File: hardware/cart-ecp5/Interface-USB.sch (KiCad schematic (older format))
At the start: 40 parts, among them U3 USBLC6-2SC6

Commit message: Replace FT2232HL with FT2232HQ for QFN-64 package
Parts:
- removed U?: FT2232HL, Package_QFP:LQFP-64_10x10mm_P0.5mm, symbol ng_ftdi:FT2232H
- added U?: FT2232HQ, Package_DFN_QFN:QFN-64-1EP_9x9mm_P0.5mm_EP4.35x4.35mm, symbol ng_ftdi:FT2232HQ
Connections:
- wire segments 191 -> 193
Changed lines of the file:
@@
 Connection ~ 9150 1350
 Wire Wire Line
-	9200 5850 9200 5950
-Wire Wire Line
-	9200 5950 9100 5950
+	9150 5850 9150 5950
+Wire Wire Line
+	9150 5950 9050 5950
 Wire Wire Line
 	7450 5550 7550 5550
 Wire Wire Line
-	8300 5850 8300 5950
-Connection ~ 8300 5950
-Wire Wire Line
-	8500 5850 8500 5950
-Connection ~ 8500 5950
-Wire Wire Line
-	8600 5850 8600 5950
-Connection ~ 8600 5950
-Wire Wire Line
-	8600 5950 8500 5950
-Wire Wire Line
-	8700 5850 8700 5950
-Connection ~ 8700 5950
-Wire Wire Line
-	8700 5950 8600 5950
-Wire Wire Line
-	8800 5850 8800 5950
-Connection ~ 8800 5950
-Wire Wire Line
-	8800 5950 8700 5950
-Wire Wire Line
-	8900 5850 8900 5950
-Connection ~ 8900 5950
-Wire Wire Line
-	8900 5950 8800 5950
-Wire Wire Line
-	9000 5850 9000 5950
-Connection ~ 9000 5950
-Wire Wire Line
-	9000 5950 8900 5950
-Wire Wire Line
-	9100 5850 9100 5950
-Connection ~ 9100 5950
-Wire Wire Line
-	9100 5950 9000 5950
+	8250 5850 8250 5950
+Connection ~ 8250 5950
+Wire Wire Line
+	8450 5850 8450 5950
+Connection ~ 8450 5950
+Wire Wire Line
+	8550 5850 8550 5950
+Connection ~ 8550 5950
+Wire Wire Line
+	8550 5950 8450 5950
+Wire Wire Line
+	8650 5850 8650 5950
+Connection ~ 8650 5950
+Wire Wire Line
+	8650 5950 8550 5950
+Wire Wire Line
+	8750 5850 8750 5950
+Connection ~ 8750 5950
+Wire Wire Line
+	8750 5950 8650 5950
+Wire Wire Line
+	8850 5850 8850 5950
+Connection ~ 8850 5950
+Wire Wire Line
+	8850 5950 8750 5950
+Wire Wire Line
+	8950 5850 8950 5950
+Connection ~ 8950 5950
+Wire Wire Line
+	8950 5950 8850 5950
+Wire Wire Line
+	9050 5850 9050 5950
+Connection ~ 9050 5950
+Wire Wire Line
+	9050 5950 8950 5950
 NoConn ~ 7550 5050
 NoConn ~ 9950 5350
@@
 Connection ~ 8950 1350
 Wire Wire Line
-	8500 5950 8300 5950
-Wire Wire Line
-	8300 5950 8300 6050
+	8450 5950 8250 5950
+Wire Wire Line
+	8250 5950 8250 6050
 Wire Wire Line
 	7450 5550 7450 5650
@@
 Wire Wire Line
 	4300 6400 4300 6500
-$Comp
-L ng_ftdi:FT2232H U?
-U 1 1 5F212584
-P 8750 3650
-F 0 "U?" H 7700 5850 50  0000 L CNN
-F 1 "FT2232HL" H 7700 5750 50  0000 L CNN
-F 2 "Package_QFP:LQFP-64_10x10mm_P0.5mm" H 8750 3650 50  0001 C CNN
-F 3 "https://www.ftdichip.com/Support/Documents/DataSheets/ICs/DS_FT2232H.pdf" H 8750 3650 50  0001 C CNN
-	1    8750 3650
-	1    0    0    -1
-$EndComp
 Wire Wire Line
 	7450 2950 7550 2950
@@
 L ng_power:GND #PWR0113
 U 1 1 5F44E9B1
-P 8300 6050
+P 8250 6050
 AR Path="/5F44E9B1" Ref="#PWR0113"  Part="1"
 AR Path="/5F302051/5F44E9B1" Ref="#PWR?"  Part="1"
 AR Path="/5F4552C5/5F44E9B1" Ref="#PWR?"  Part="1"
-F 0 "#PWR?" H 8300 5800 50  0001 C CNN
-F 1 "GND" H 8303 5924 50  0000 C CNN
-F 2 "" H 8200 5700 50  0001 C CNN
-F 3 "" H 8300 6050 50  0001 C CNN
-	1    8300 6050
+F 0 "#PWR?" H 8250 5800 50  0001 C CNN
+F 1 "GND" H 8253 5924 50  0000 C CNN
+F 2 "" H 8150 5700 50  0001 C CNN
+F 3 "" H 8250 6050 50  0001 C CNN
+	1    8250 6050
 	1    0    0    -1
 $EndComp
@@
 	1    0    0    -1
 $EndComp
+$Comp
+L ng_ftdi:FT2232HQ U?
+U 1 1 5F48BD9E
+P 8750 3650
+F 0 "U?" H 7700 5850 50  0000 L CNN
+F 1 "FT2232HQ" H 7700 5750 50  0000 L CNN
+F 2 "Package_DFN_QFN:QFN-64-1EP_9x9mm_P0.5mm_EP4.35x4.35mm" H 8750 3650 50  0001 C CNN
+F 3 "https://www.ftdichip.com/Support/Documents/DataSheets/ICs/DS_FT2232H.pdf" H 8750 3650 50  0001 C CNN
+	1    8750 3650
+	1    0    0    -1
+$EndComp
+Wire Wire Line
+	9150 5950 9250 5950
+Wire Wire Line
+	9250 5950 9250 5850
+Connection ~ 9150 5950
 $EndSCHEMATC

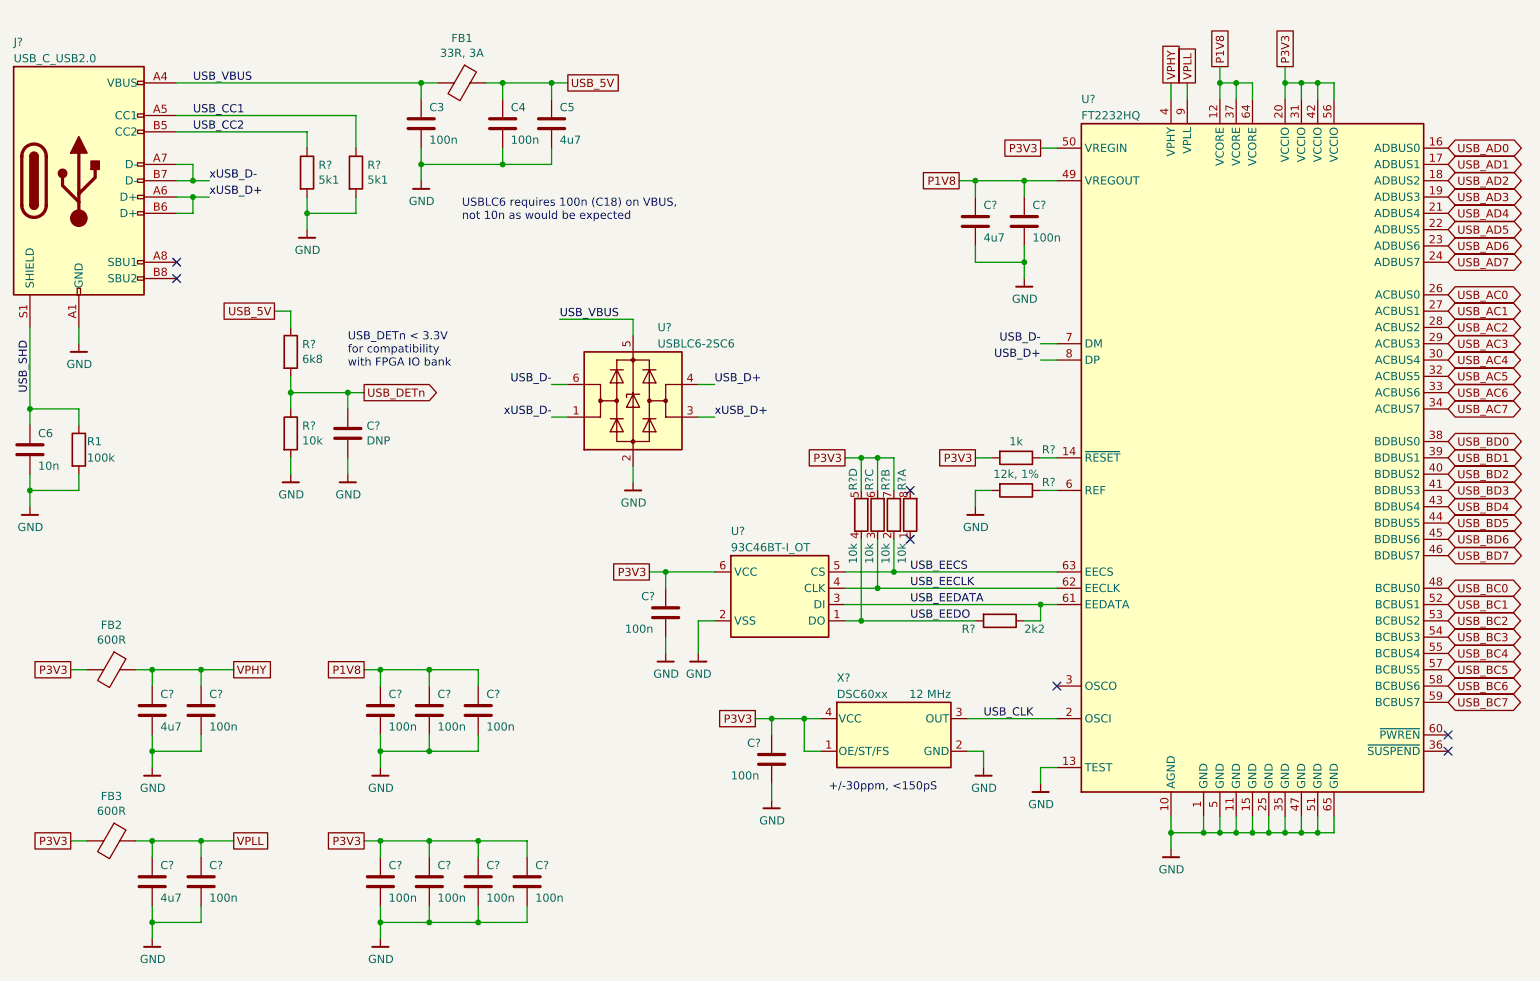
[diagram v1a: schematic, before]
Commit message: First pass annotation and footprint assignment complete
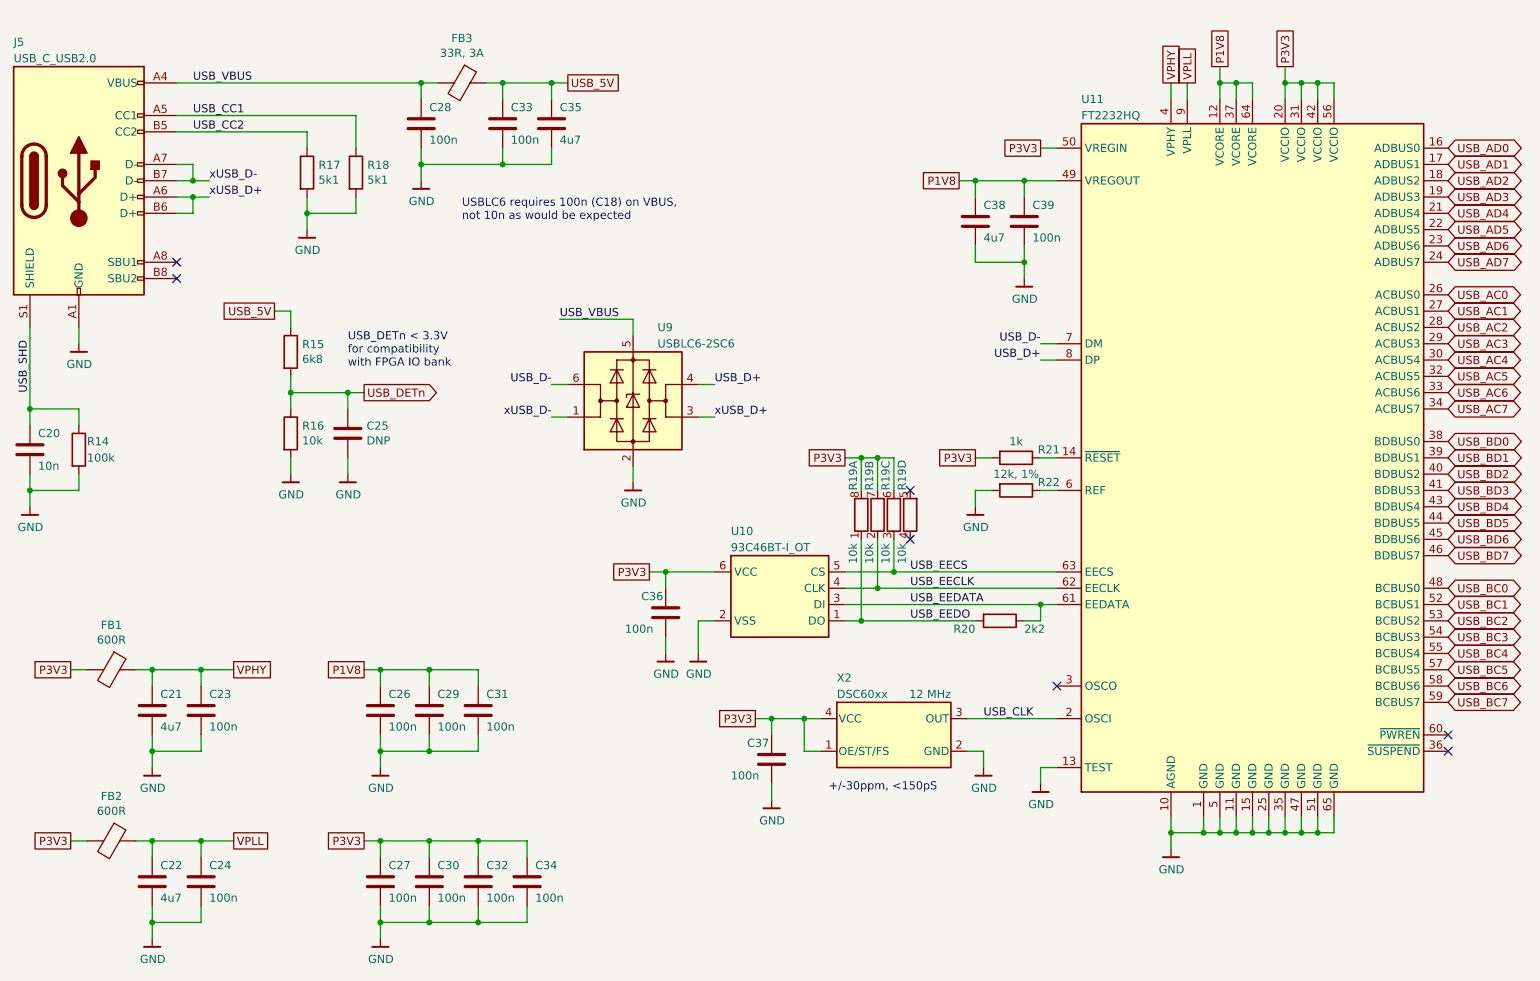
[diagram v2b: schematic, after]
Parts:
- gave numbers to parts that had none: 26
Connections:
- net P3V3: now also R19.6 (R3.2), R19.7 (R2.2), R19.8 (R1.2); no longer R19.5 (R4.2), R19.6 (R3.2), R19.7 (R2.2)
- net USB_EECLK: now also R19.2 (R2.1); no longer R19.3 (R3.1)
- net USB_EECS: now also R19.3 (R3.1); no longer R19.2 (R2.1)
- net USB_EEDO: now also R19.1 (R1.1); no longer R19.4 (R4.1)

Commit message: Initial placement pass
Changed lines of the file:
@@
 	5350 4650 5350 4850
 Wire Wire Line
-	6350 3650 6250 3650
-Connection ~ 6450 3650
-Wire Wire Line
-	6350 3650 6350 3850
-Wire Wire Line
-	6450 3650 6550 3650
-Wire Wire Line
-	6450 3650 6450 3850
-Wire Wire Line
-	6350 3650 6450 3650
-Wire Wire Line
-	6550 3850 6550 3650
+	6350 3550 6250 3550
+Connection ~ 6450 3550
+Wire Wire Line
+	6350 3550 6350 3850
+Wire Wire Line
+	6450 3550 6550 3550
+Wire Wire Line
+	6450 3550 6450 3850
+Wire Wire Line
+	6350 3550 6450 3550
+Wire Wire Line
+	6550 3850 6550 3550
 Wire Wire Line
 	6450 4450 6450 4150
@@
 Wire Wire Line
 	6250 4350 6550 4350
-Connection ~ 6350 3650
+Connection ~ 6350 3550
 Wire Wire Line
 	7550 4550 7450 4550
@@
 Text GLabel 3300 6000 0    50   UnSpc ~ 0
 P3V3
-Text GLabel 6250 3650 0    50   UnSpc ~ 0
+Text GLabel 6250 3550 0    50   UnSpc ~ 0
 P3V3
 $Comp

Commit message: Shrink smallest passive to 0402
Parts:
- C23, C24, C25, C26, C27, C29, C3, C30, C31, C32, C34, C36, C37, C39, C4, C6: footprint Capacitor_SMD:C_0603_1608Metric -> Capacitor_SMD:C_0402_1005Metric
- FB1: value 33R, 3A -> 33R; footprint Inductor_SMD:L_0603_1608Metric -> Inductor_SMD:L_0402_1005Metric; MPN BLM18PG330SN1D -> (none)
- FB2, FB3: footprint Inductor_SMD:L_0603_1608Metric -> Inductor_SMD:L_0402_1005Metric
- R1: footprint Resistor_SMD:R_0603_1608Metric -> Resistor_SMD:R_0402_1005Metric; MPN RC0603JR-07100KL -> (none)
- R17, R18, R20, R21, R22: footprint Resistor_SMD:R_0603_1608Metric -> Resistor_SMD:R_0402_1005Metric
- R19: footprint Resistor_SMD:R_Array_Convex_4x0603 -> Resistor_SMD:R_0402_1005Metric; symbol Device:R_Pack04_Split -> Device:R; MPN YC164-JR-0710KL -> (none)
- R23, R24: renamed from R19; footprint Resistor_SMD:R_Array_Convex_4x0603 -> Resistor_SMD:R_0402_1005Metric; symbol Device:R_Pack04_Split -> Device:R
- R25: renamed from R19; footprint Resistor_SMD:R_Array_Convex_4x0603 -> Resistor_SMD:R_0402_1005Metric; symbol Device:R_Pack04_Split -> Device:R; MPN YC164-JR-0710KL -> (none)
- R3: footprint Resistor_SMD:R_0603_1608Metric -> Resistor_SMD:R_0402_1005Metric; MPN RC0603FR-076K8L -> (none)
- R5: footprint Resistor_SMD:R_0603_1608Metric -> Resistor_SMD:R_0402_1005Metric; MPN RC0603FR-0710KL -> (none)
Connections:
- net P3V3: now also R19.1, R23.1, R24.1; no longer R19.8 (R1.2), R23.7 (R2.2), R24.6 (R3.2)
- net USB_EECS: now also R24.2; no longer R24.3 (R3.1)
- net USB_EEDO: now also R19.2; no longer R19.1 (R1.1)
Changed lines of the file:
@@
 U 1 1 5F1F46DB
 P 5150 4600
-F 0 "C36" H 5000 4700 50  0000 L CNN
+F 0 "C36" H 4950 4700 50  0000 L CNN
 F 1 "100n" H 4900 4500 50  0000 L CNN
-F 2 "Capacitor_SMD:C_0603_1608Metric" H 5188 4450 50  0001 C CNN
+F 2 "Capacitor_SMD:C_0402_1005Metric" H 5188 4450 50  0001 C CNN
 F 3 "~" H 5150 4600 50  0001 C CNN
 	1    5150 4600
@@
 	6550 4350 6550 4150
 $Comp
-L Device:R_Pack04_Split R19
-U 4 1 5F1F46F9
+L Device:R R25
+U 1 1 5F1F46F9
 P 6650 4000
-F 0 "R19" V 6600 4150 50  0000 L CNN
+F 0 "R25" V 6600 4150 50  0000 L CNN
 F 1 "10k" V 6600 3700 50  0000 L CNN
-F 2 "Resistor_SMD:R_Array_Convex_4x0603" V 6580 4000 50  0001 C CNN
+F 2 "Resistor_SMD:R_0402_1005Metric" V 6580 4000 50  0001 C CNN
 F 3 "~" H 6650 4000 50  0001 C CNN
-F 4 "YC164-JR-0710KL" V 6650 4000 50  0001 C CNN "MPN"
-	4    6650 4000
-	1    0    0    -1
-$EndComp
-$Comp
-L Device:R_Pack04_Split R19
-U 2 1 5F1F46FF
+F 4 "" V 6650 4000 50  0001 C CNN "MPN"
+	1    6650 4000
+	1    0    0    -1
+$EndComp
+$Comp
+L Device:R R23
+U 1 1 5F1F46FF
 P 6450 4000
-F 0 "R19" V 6400 4150 50  0000 L CNN
+F 0 "R23" V 6400 4150 50  0000 L CNN
 F 1 "10k" V 6400 3700 50  0000 L CNN
-F 2 "Resistor_SMD:R_Array_Convex_4x0603" V 6380 4000 50  0001 C CNN
+F 2 "Resistor_SMD:R_0402_1005Metric" V 6380 4000 50  0001 C CNN
 F 3 "~" H 6450 4000 50  0001 C CNN
-	2    6450 4000
-	1    0    0    -1
-$EndComp
-$Comp
-L Device:R_Pack04_Split R19
-U 3 1 5F1F4705
+	1    6450 4000
+	1    0    0    -1
+$EndComp
+$Comp
+L Device:R R24
+U 1 1 5F1F4705
 P 6550 4000
-F 0 "R19" V 6500 4150 50  0000 L CNN
+F 0 "R24" V 6500 4150 50  0000 L CNN
 F 1 "10k" V 6500 3700 50  0000 L CNN
-F 2 "Resistor_SMD:R_Array_Convex_4x0603" V 6480 4000 50  0001 C CNN
+F 2 "Resistor_SMD:R_0402_1005Metric" V 6480 4000 50  0001 C CNN
 F 3 "~" H 6550 4000 50  0001 C CNN
-	3    6550 4000
+	1    6550 4000
 	1    0    0    -1
 $EndComp
@@
 U 1 1 5F1F476F
 P 5800 5500
-F 0 "C37" H 5650 5600 50  0000 L CNN
+F 0 "C37" H 5600 5600 50  0000 L CNN
 F 1 "100n" H 5550 5400 50  0000 L CNN
-F 2 "Capacitor_SMD:C_0603_1608Metric" H 5838 5350 50  0001 C CNN
+F 2 "Capacitor_SMD:C_0402_1005Metric" H 5838 5350 50  0001 C CNN
 F 3 "~" H 5800 5500 50  0001 C CNN
 	1    5800 5500
@@
 F 0 "C39" H 7300 2300 50  0000 R CNN
 F 1 "100n" H 7300 2100 50  0000 R CNN
-F 2 "Capacitor_SMD:C_0603_1608Metric" H 7388 2050 50  0001 C CNN
+F 2 "Capacitor_SMD:C_0402_1005Metric" H 7388 2050 50  0001 C CNN
 F 3 "~" H 7350 2200 50  0001 C CNN
 	1    7350 2200
@@
 F 0 "C23" H 2350 5300 50  0000 L CNN
 F 1 "100n" H 2350 5100 50  0000 L CNN
-F 2 "Capacitor_SMD:C_0603_1608Metric" H 2338 5050 50  0001 C CNN
+F 2 "Capacitor_SMD:C_0402_1005Metric" H 2338 5050 50  0001 C CNN
 F 3 "~" H 2300 5200 50  0001 C CNN
 	1    2300 5200
@@
 F 0 "R20" V 7250 4500 50  0000 R CNN
 F 1 "2k2" V 7250 4800 50  0000 L CNN
-F 2 "Resistor_SMD:R_0603_1608Metric" V 7130 4650 50  0001 C CNN
+F 2 "Resistor_SMD:R_0402_1005Metric" V 7130 4650 50  0001 C CNN
 F 3 "~" H 7200 4650 50  0001 C CNN
 	1    7200 4650
@@
 F 0 "C33" H 4200 1700 50  0000 L CNN
 F 1 "100n" H 4200 1500 50  0000 L CNN
-F 2 "Capacitor_SMD:C_0603_1608Metric" H 4188 1450 50  0001 C CNN
+F 2 "Capacitor_SMD:C_0402_1005Metric" H 4188 1450 50  0001 C CNN
 F 3 "~" H 4150 1600 50  0001 C CNN
 F 4 "" H 4150 1600 50  0001 C CNN "MPN"
@@
 F 0 "R14" H 1600 3650 50  0000 L CNN
 F 1 "100k" H 1600 3550 50  0000 L CNN
-F 2 "Resistor_SMD:R_0603_1608Metric" V 1480 3600 50  0001 C CNN
+F 2 "Resistor_SMD:R_0402_1005Metric" V 1480 3600 50  0001 C CNN
 F 3 "~" H 1550 3600 50  0001 C CNN
-F 4 "RC0603JR-07100KL" H 1550 3600 50  0001 C CNN "MPN"
+F 4 "" H 1550 3600 50  0001 C CNN "MPN"
 	1    1550 3600
 	1    0    0    -1
@@
 F 0 "C20" H 1300 3700 50  0000 L CNN
 F 1 "10n" H 1300 3500 50  0000 L CNN
-F 2 "Capacitor_SMD:C_0603_1608Metric" H 1288 3450 50  0001 C CNN
+F 2 "Capacitor_SMD:C_0402_1005Metric" H 1288 3450 50  0001 C CNN
 F 3 "~" H 1250 3600 50  0001 C CNN
 F 4 "" H 1250 3600 50  0001 C CNN "MPN"
@@
 AR Path="/5F4552C5/5F184C3D" Ref="FB3"  Part="1"
 F 0 "FB3" V 3626 1350 50  0000 C CNN
-F 1 "33R, 3A" V 3717 1350 50  0000 C CNN
-F 2 "Inductor_SMD:L_0603_1608Metric" V 3830 1350 50  0001 C CNN
+F 1 "33R" V 3717 1350 50  0000 C CNN
+F 2 "Inductor_SMD:L_0402_1005Metric" V 3830 1350 50  0001 C CNN
 F 3 "~" H 3900 1350 50  0001 C CNN
-F 4 "BLM18PG330SN1D" V 3900 1350 50  0001 C CNN "MPN"
 	1    3900 1350
 	0    1    1    0
@@
 F 0 "C28" H 3700 1700 50  0000 L CNN
 F 1 "100n" H 3700 1500 50  0000 L CNN
-F 2 "Capacitor_SMD:C_0603_1608Metric" H 3688 1450 50  0001 C CNN
+F 2 "Capacitor_SMD:C_0402_1005Metric" H 3688 1450 50  0001 C CNN
 F 3 "~" H 3650 1600 50  0001 C CNN
 F 4 "" H 3650 1600 50  0001 C CNN "MPN"
@@
 F 0 "C24" H 2350 6350 50  0000 L CNN
 F 1 "100n" H 2350 6150 50  0000 L CNN
-F 2 "Capacitor_SMD:C_0603_1608Metric" H 2338 6100 50  0001 C CNN
+F 2 "Capacitor_SMD:C_0402_1005Metric" H 2338 6100 50  0001 C CNN
 F 3 "~" H 2300 6250 50  0001 C CNN
 	1    2300 6250
@@
 F 0 "C26" H 3450 5300 50  0000 L CNN
 F 1 "100n" H 3450 5100 50  0000 L CNN
-F 2 "Capacitor_SMD:C_0603_1608Metric" H 3438 5050 50  0001 C CNN
+F 2 "Capacitor_SMD:C_0402_1005Metric" H 3438 5050 50  0001 C CNN
 F 3 "~" H 3400 5200 50  0001 C CNN
 	1    3400 5200
@@
 F 0 "C29" H 3750 5300 50  0000 L CNN
 F 1 "100n" H 3750 5100 50  0000 L CNN
-F 2 "Capacitor_SMD:C_0603_1608Metric" H 3738 5050 50  0001 C CNN
+F 2 "Capacitor_SMD:C_0402_1005Metric" H 3738 5050 50  0001 C CNN
 F 3 "~" H 3700 5200 50  0001 C CNN
 	1    3700 5200
@@
 F 0 "C31" H 4050 5300 50  0000 L CNN
 F 1 "100n" H 4050 5100 50  0000 L CNN
-F 2 "Capacitor_SMD:C_0603_1608Metric" H 4038 5050 50  0001 C CNN
+F 2 "Capacitor_SMD:C_0402_1005Metric" H 4038 5050 50  0001 C CNN
 F 3 "~" H 4000 5200 50  0001 C CNN
 	1    4000 5200
@@
 F 0 "C34" H 4350 6350 50  0000 L CNN
 F 1 "100n" H 4350 6150 50  0000 L CNN
-F 2 "Capacitor_SMD:C_0603_1608Metric" H 4338 6100 50  0001 C CNN
+F 2 "Capacitor_SMD:C_0402_1005Metric" H 4338 6100 50  0001 C CNN
 F 3 "~" H 4300 6250 50  0001 C CNN
 	1    4300 6250
@@
 F 0 "C32" H 4050 6350 50  0000 L CNN
 F 1 "100n" H 4050 6150 50  0000 L CNN
-F 2 "Capacitor_SMD:C_0603_1608Metric" H 4038 6100 50  0001 C CNN
+F 2 "Capacitor_SMD:C_0402_1005Metric" H 4038 6100 50  0001 C CNN
 F 3 "~" H 4000 6250 50  0001 C CNN
 	1    4000 6250
@@
 F 0 "C30" H 3750 6350 50  0000 L CNN
 F 1 "100n" H 3750 6150 50  0000 L CNN
-F 2 "Capacitor_SMD:C_0603_1608Metric" H 3738 6100 50  0001 C CNN
+F 2 "Capacitor_SMD:C_0402_1005Metric" H 3738 6100 50  0001 C CNN
 F 3 "~" H 3700 6250 50  0001 C CNN
 	1    3700 6250
@@
 F 0 "C27" H 3450 6350 50  0000 L CNN
 F 1 "100n" H 3450 6150 50  0000 L CNN
-F 2 "Capacitor_SMD:C_0603_1608Metric" H 3438 6100 50  0001 C CNN
+F 2 "Capacitor_SMD:C_0402_1005Metric" H 3438 6100 50  0001 C CNN
 F 3 "~" H 3400 6250 50  0001 C CNN
 	1    3400 6250
@@
 F 0 "FB1" V 1476 4950 50  0000 C CNN
 F 1 "600R" V 1567 4950 50  0000 C CNN
-F 2 "Inductor_SMD:L_0603_1608Metric" V 1680 4950 50  0001 C CNN
+F 2 "Inductor_SMD:L_0402_1005Metric" V 1680 4950 50  0001 C CNN
 F 3 "~" H 1750 4950 50  0001 C CNN
 F 4 "" V 1750 4950 50  0001 C CNN "MPN"
@@
 F 0 "FB2" V 1476 6000 50  0000 C CNN
 F 1 "600R" V 1567 6000 50  0000 C CNN
-F 2 "Inductor_SMD:L_0603_1608Metric" V 1680 6000 50  0001 C CNN
+F 2 "Inductor_SMD:L_0402_1005Metric" V 1680 6000 50  0001 C CNN
 F 3 "~" H 1750 6000 50  0001 C CNN
 F 4 "" V 1750 6000 50  0001 C CNN "MPN"
@@
 NoConn ~ 6650 3850
 $Comp
-L Device:R_Pack04_Split R19
+L Device:R R19
 U 1 1 5FBDF481
 P 6350 4000
 F 0 "R19" V 6300 4150 50  0000 L CNN
 F 1 "10k" V 6300 3700 50  0000 L CNN
-F 2 "Resistor_SMD:R_Array_Convex_4x0603" V 6280 4000 50  0001 C CNN
+F 2 "Resistor_SMD:R_0402_1005Metric" V 6280 4000 50  0001 C CNN
 F 3 "~" H 6350 4000 50  0001 C CNN
-F 4 "YC164-JR-0710KL" V 6350 4000 50  0001 C CNN "MPN"
+F 4 "" V 6350 4000 50  0001 C CNN "MPN"
 	1    6350 4000
 	1    0    0    -1
@@
 F 0 "R22" V 7250 4050 50  0000 C CNN
 F 1 "12k, 1%" V 7200 3850 50  0000 C CNN
-F 2 "Resistor_SMD:R_0603_1608Metric" V 7230 3850 50  0001 C CNN
+F 2 "Resistor_SMD:R_0402_1005Metric" V 7230 3850 50  0001 C CNN
 F 3 "~" H 7300 3850 50  0001 C CNN
 	1    7300 3850
@@
 F 0 "R21" V 7250 3850 50  0000 C CNN
 F 1 "1k" V 7200 3650 50  0000 C CNN
-F 2 "Resistor_SMD:R_0603_1608Metric" V 7230 3650 50  0001 C CNN
+F 2 "Resistor_SMD:R_0402_1005Metric" V 7230 3650 50  0001 C CNN
 F 3 "~" H 7300 3650 50  0001 C CNN
 	1    7300 3650
@@
 F 0 "R17" H 3020 1946 50  0000 L CNN
 F 1 "5k1" H 3020 1855 50  0000 L CNN
-F 2 "Resistor_SMD:R_0603_1608Metric" V 2880 1900 50  0001 C CNN
+F 2 "Resistor_SMD:R_0402_1005Metric" V 2880 1900 50  0001 C CNN
 F 3 "~" H 2950 1900 50  0001 C CNN
 	1    2950 1900
@@
 F 0 "R18" H 3320 1946 50  0000 L CNN
 F 1 "5k1" H 3320 1855 50  0000 L CNN
-F 2 "Resistor_SMD:R_0603_1608Metric" V 3180 1900 50  0001 C CNN
+F 2 "Resistor_SMD:R_0402_1005Metric" V 3180 1900 50  0001 C CNN
 F 3 "~" H 3250 1900 50  0001 C CNN
 	1    3250 1900
@@
 F 0 "R15" H 2920 3046 50  0000 L CNN
 F 1 "6k8" H 2920 2955 50  0000 L CNN
-F 2 "Resistor_SMD:R_0603_1608Metric" V 2780 3000 50  0001 C CNN
+F 2 "Resistor_SMD:R_0402_1005Metric" V 2780 3000 50  0001 C CNN
 F 3 "~" H 2850 3000 50  0001 C CNN
-F 4 "RC0603FR-076K8L" H 2850 3000 50  0001 C CNN "MPN"
+F 4 "" H 2850 3000 50  0001 C CNN "MPN"
 	1    2850 3000
 	1    0    0    -1
@@
 F 0 "R16" H 2920 3546 50  0000 L CNN
 F 1 "10k" H 2920 3455 50  0000 L CNN
-F 2 "Resistor_SMD:R_0603_1608Metric" V 2780 3500 50  0001 C CNN
+F 2 "Resistor_SMD:R_0402_1005Metric" V 2780 3500 50  0001 C CNN
 F 3 "~" H 2850 3500 50  0001 C CNN
-F 4 "RC0603FR-0710KL" H 2850 3500 50  0001 C CNN "MPN"
+F 4 "" H 2850 3500 50  0001 C CNN "MPN"
 	1    2850 3500
 	1    0    0    -1
@@
 F 0 "C25" H 3315 3546 50  0000 L CNN
 F 1 "DNP" H 3315 3455 50  0000 L CNN
-F 2 "Capacitor_SMD:C_0603_1608Metric" H 3238 3350 50  0001 C CNN
+F 2 "Capacitor_SMD:C_0402_1005Metric" H 3238 3350 50  0001 C CNN
 F 3 "~" H 3200 3500 50  0001 C CNN
 	1    3200 3500
